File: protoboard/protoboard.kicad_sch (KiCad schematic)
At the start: 8 parts, among them J1 Conn_01x19_Pin, J2 Conn_01x19_Pin, SW1 RotaryEncoder_Switch, U1 ESP32-DEVKITC-32D

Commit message: finish protoboard v1
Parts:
- removed J1, J2: Conn_01x19_Pin, symbol Connector:Conn_01x19_Pin
- removed U1: ESP32-DEVKITC-32D, ESP32-DEVKITC-32D:MODULE_ESP32-DEVKITC-32D, symbol ESP32-DEVKITC-32D:ESP32-DEVKITC-32D
- added J1: Conn_01x18_Pin, symbol Connector:Conn_01x18_Pin
- added J2: Barrel_Jack, symbol Connector:Barrel_Jack
- added J5: Conn_01x04_Pin, symbol Connector:Conn_01x04_Pin
- added U1: TPSM84203, layout:TI-SIP_3, symbol CalSol_power:TPSM84205
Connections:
- net +3V3: now also J1.1 (Pin_1), J5.1 (Pin_1), U1.3 (VOUT)
- net A: now also J1.3 (Pin_3)
- net B: now also J1.5 (Pin_5)
- net ENC_SW: now also J1.4 (Pin_4)
- net GND: now also J1.2 (Pin_2), J2.2, J5.2 (Pin_2), U1.2 (GND)
- net LED_RGB1_B: now also J1.8 (Pin_8)
- net LED_RGB1_G: now also J1.9 (Pin_9)
- net LED_RGB1_R: now also J1.10 (Pin_10)
- net PWM: now also J1.18 (Pin_18)
- net VOC: now also J1.17 (Pin_17)
- net VOUT: now also J1.15 (Pin_15)
- net VREF: now also J1.14 (Pin_14)
- net VS: now also J1.12 (Pin_12)
- net ~{ALERT}: now also J1.16 (Pin_16)
- net ~{FLT}: now also J1.11 (Pin_11)
- net ~{OC}: now also J1.13 (Pin_13)
- new net +12V: J2.1, U1.1 (VIN)
- new net SCL: J1.6 (Pin_6), J5.3 (Pin_3)
- new net SDA: J1.7 (Pin_7), J5.4 (Pin_4)
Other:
- note added: "Current Sense"
- note added: "Input"
- note added: "OLED"
- note added: "Output"
- note added: "Pins to ESP32"
- note added: "Power Management"
- moved on the sheet: D3, R1, R2, R3, SW1

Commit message: footprint update
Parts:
- J2: footprint (none) -> Connector_BarrelJack:BarrelJack_Horizontal
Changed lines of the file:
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@@
 			)
 		)
-		(property "Footprint" ""
+		(property "Footprint" "Connector_BarrelJack:BarrelJack_Horizontal"
 			(at 60.96 115.316 0)
 			(effects

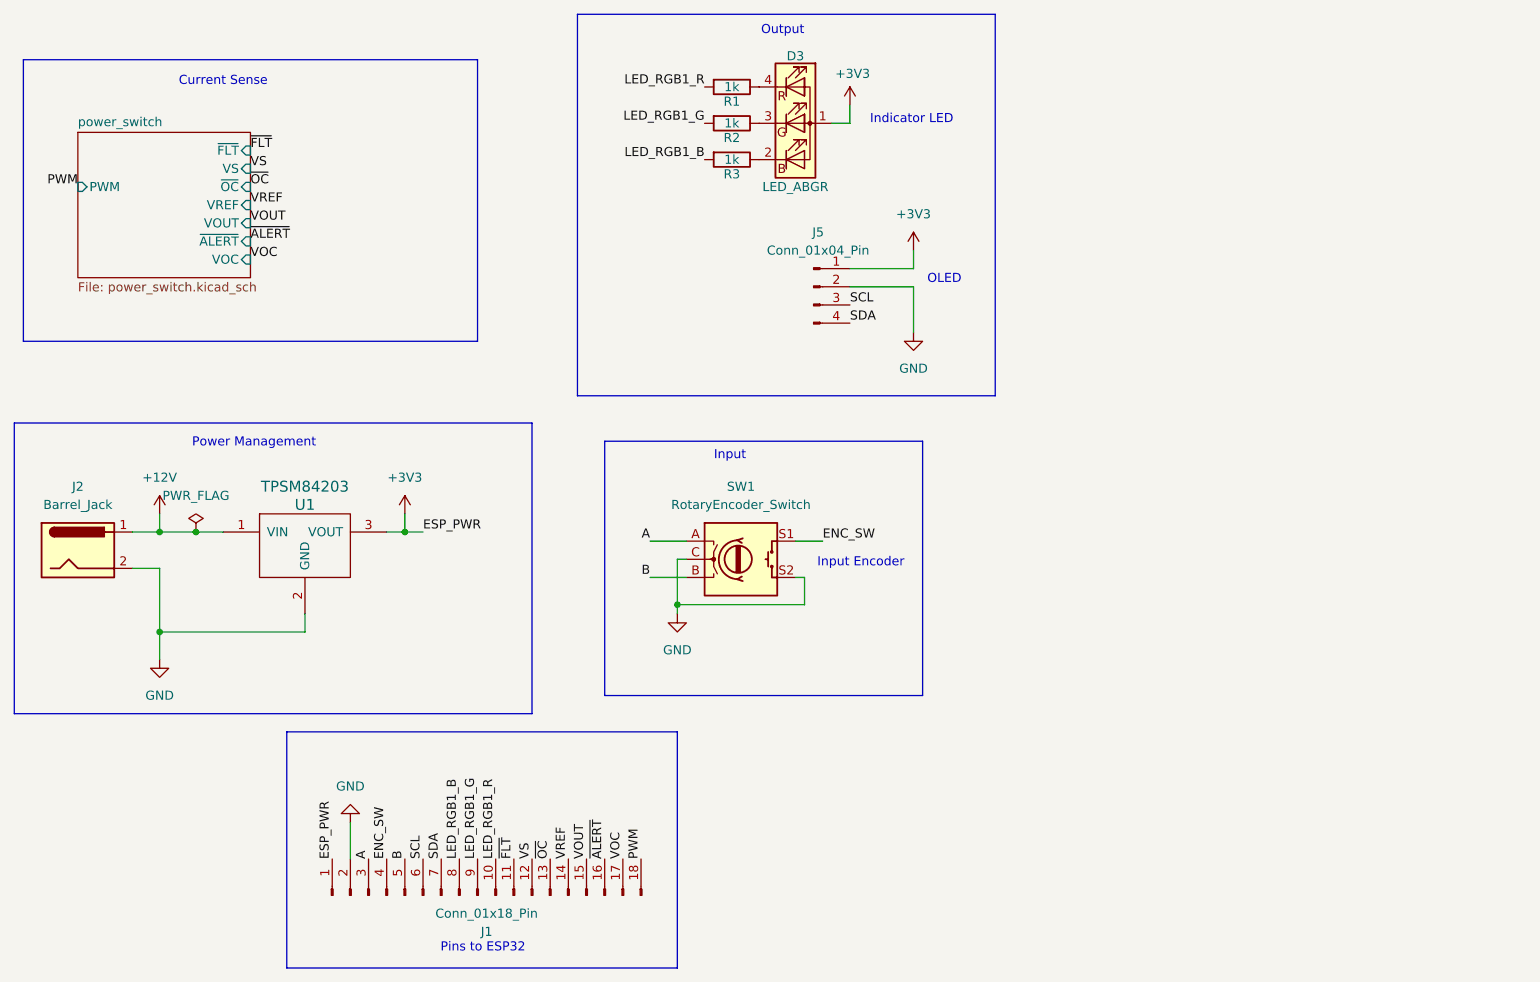
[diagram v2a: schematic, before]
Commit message: schematic review changes
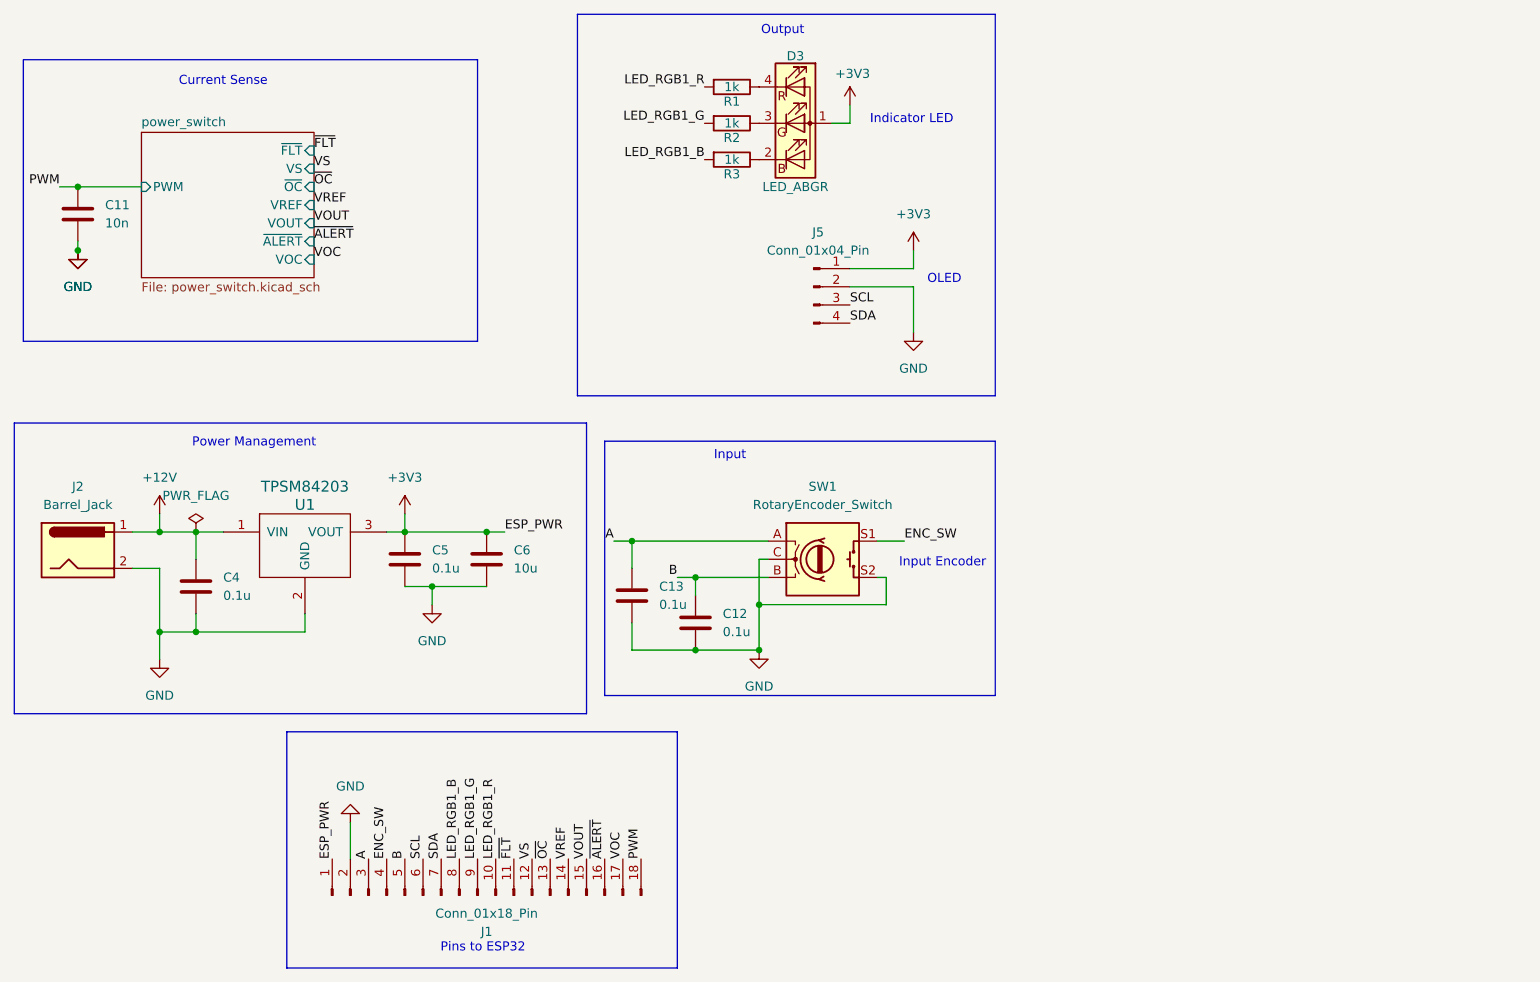
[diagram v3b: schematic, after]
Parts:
- added C11: 10n, Capacitor_SMD:C_0603_1608Metric, symbol Device:C
- added C12, C13, C4, C5: 0.1u, Capacitor_SMD:C_0603_1608Metric, symbol Device:C
- added C6: 10u, Capacitor_SMD:C_0603_1608Metric, symbol Device:C
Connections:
- net +12V: now also C4.1
- net +3V3: now also C5.1, C6.1
- net A: now also C13.1
- net B: now also C12.1
- net GND: now also C11.2, C12.2, C13.2, C4.2, C5.2, C6.2
- net PWM: now also C11.1
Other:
- moved on the sheet: SW1

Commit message: forgot to save sch file
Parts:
- removed J2: Barrel_Jack, Connector_BarrelJack:BarrelJack_Horizontal, symbol Connector:Barrel_Jack
- added J2: Conn_01x02_Socket, symbol Connector:Conn_01x02_Socket
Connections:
- net +12V: now also J2.2 (Pin_2)
- net GND: now also J2.1 (Pin_1)
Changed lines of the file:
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@@
 	(wire
 		(pts
-			(xy 71.12 116.84) (xy 71.12 125.73)
+			(xy 71.12 114.3) (xy 71.12 125.73)
 		)
 		(stroke
@@
 	(wire
 		(pts
+			(xy 71.12 114.3) (xy 67.31 114.3)
+		)
+		(stroke
+			(width 0)
+			(type default)
+		)
+	)
+	(wire
+		(pts
 			(xy 172.72 118.11) (xy 172.72 121.92)
 		)
@@
 		(pts
 			(xy 137.16 128.27) (xy 146.05 128.27)
-		)
-		(stroke
-			(width 0)
-			(type default)
-		)
-	)
-	(wire
-		(pts
-			(xy 71.12 116.84) (xy 67.31 116.84)
 		)
 		(stroke
@@
 			)
 			(justify left bottom)
+		)
+	)
+	(symbol
+		(lib_id "Connector:Conn_01x02_Socket")
+		(at 62.23 114.3 180)
+		(unit 1)
+		(exclude_from_sim no)
+		(in_bom yes)
+		(on_board yes)
+		(dnp no)
+		(fields_autoplaced yes)
+		(property "Reference" "J2"
+			(at 62.865 106.68 0)
+			(effects
+				(font
+					(size 1.27 1.27)
+				)
+			)
+		)
+		(property "Value" "Conn_01x02_Socket"
+			(at 62.865 109.22 0)
+			(effects
+				(font
+					(size 1.27 1.27)
+				)
+			)
+		)
+		(property "Footprint" ""
+			(at 62.23 114.3 0)
+			(effects
+				(font
+					(size 1.27 1.27)
+				)
+				(hide yes)
+			)
+		)
+		(property "Datasheet" "~"
+			(at 62.23 114.3 0)
+			(effects
+				(font
+					(size 1.27 1.27)
+				)
+				(hide yes)
+			)
+		)
+		(property "Description" "Generic connector, single row, 01x02, script generated"
+			(at 62.23 114.3 0)
+			(effects
+				(font
+					(size 1.27 1.27)
+				)
+				(hide yes)
+			)
+		)
+		(pin "1"
+		)
+		(pin "2"
+		)
+		(instances
+			(project ""
+				(path "/9233c06e-90cd-4cc2-bc77-fac00ef686c2"
+					(reference "J2")
+					(unit 1)
+				)
+			)
 		)
 	)
@@
 					(unit 1)
 				)
-			)
-		)
-	)
-	(symbol
-		(lib_id "Connector:Barrel_Jack")
-		(at 59.69 114.3 0)
-		(unit 1)
-		(exclude_from_sim no)
-		(in_bom yes)
-		(on_board yes)
-		(dnp no)
-		(fields_autoplaced yes)
-		(property "Reference" "J2"
-			(at 59.69 105.41 0)
-			(effects
-				(font
-					(size 1.27 1.27)
-				)
-			)
-		)
-		(property "Value" "Barrel_Jack"
-			(at 59.69 107.95 0)
-			(effects
-				(font
-					(size 1.27 1.27)
-				)
-			)
-		)
-		(property "Footprint" "Connector_BarrelJack:BarrelJack_Horizontal"
-			(at 60.96 115.316 0)
-			(effects
-				(font
-					(size 1.27 1.27)
-				)
-				(hide yes)
-			)
-		)
-		(property "Datasheet" "~"
-			(at 60.96 115.316 0)
-			(effects
-				(font
-					(size 1.27 1.27)
-				)
-				(hide yes)
-			)
-		)
-		(property "Description" "DC Barrel Jack"
-			(at 59.69 114.3 0)
-			(effects
-				(font
-					(size 1.27 1.27)
-				)
-				(hide yes)
-			)
-		)
-		(pin "1"
-		)
-		(pin "2"
-		)
-		(instances
-			(project ""
-				(path "/9233c06e-90cd-4cc2-bc77-fac00ef686c2"
-					(reference "J2")
-					(unit 1)
-				)
